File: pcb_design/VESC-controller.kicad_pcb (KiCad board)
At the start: 2 copper layers, 160 x 92.5 mm, 2 parts, among them U1 STM32F40X_LQFP64

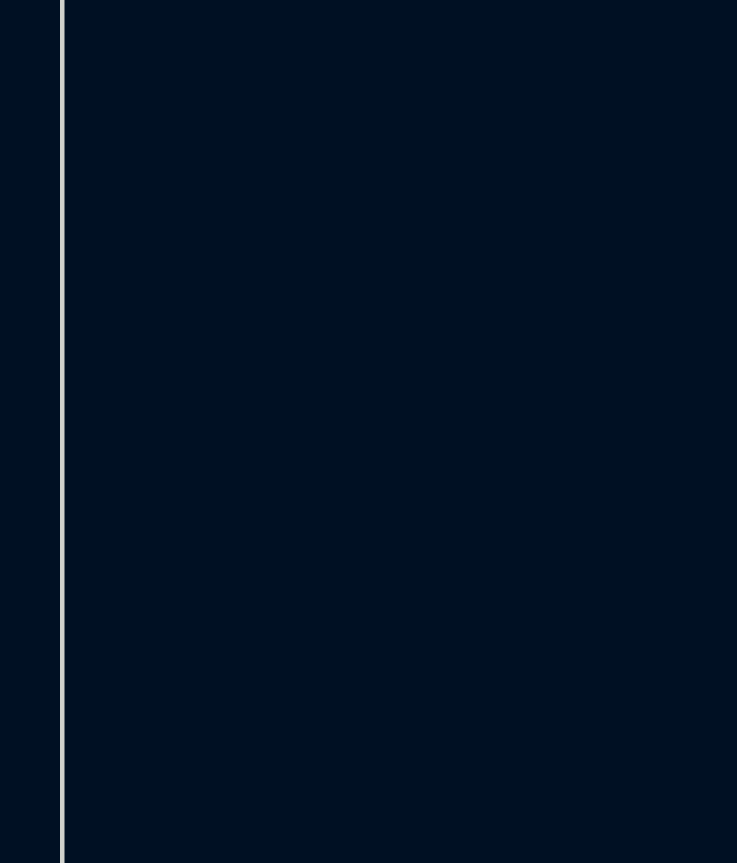
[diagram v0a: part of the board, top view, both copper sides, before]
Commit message: Added base VESC 4.xx schematic, added protection features, signal conditioning and pcb form factor
Signed-off-by: Marcos Chaparro <mchaparro@paltatech.com>
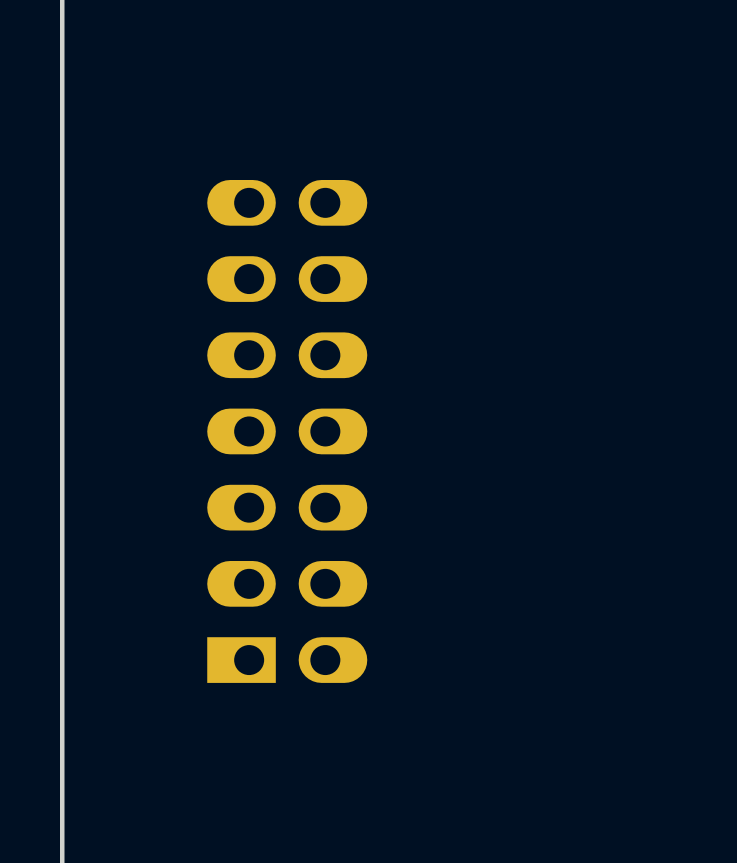
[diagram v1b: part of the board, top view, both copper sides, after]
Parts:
- added REF**: CONN-100MIL-M-2x7, conn-100mil:CONN-100MIL-M-2x7, B.Cu at (-72.5, 0.00)
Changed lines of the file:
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@@
     (links 0)
     (no_connects 0)
-    (area 0 0 0 0)
+    (area -80.275001 -45.275001 80.275001 47.775001)
     (thickness 1.6)
     (drawings 0)
     (tracks 0)
     (zones 0)
-    (modules 2)
+    (modules 3)
     (nets 65)
   )
@@
     (add_net "Net-(U1-Pad9)")
   )
+  (module conn-100mil:CONN-100MIL-M-2x7 (layer B.Cu)
+    (at -72.5 0 90)
+    (fp_text reference REF** (at 0 0 90) (layer B.SilkS)
+      (effects (font (size 0.8 0.8) (thickness 0.15)) (justify mirror))
+    )
+    (fp_text value CONN-100MIL-M-2x7 (at 0 0 90) (layer B.Fab)
+      (effects (font (size 0.8 0.8) (thickness 0.15)) (justify mirror))
+    )
+    (fp_line (start -9.525 -3.81) (end -6.35 -3.81) (layer B.SilkS) (width 0.15))
+    (fp_line (start -6.35 0) (end -6.35 -3.175) (layer B.Fab) (width 0.15))
+    (fp_line (start -9.525 0) (end -6.35 0) (layer B.Fab) (width 0.15))
+    (fp_line (start -6.35 0) (end -6.35 -3.175) (layer B.SilkS) (width 0.35))
+    (fp_line (start -9.525 0) (end -6.35 0) (layer B.SilkS) (width 0.35))
+    (fp_line (start -9.525 -3.175) (end -9.525 3.175) (layer B.SilkS) (width 0.35))
+    (fp_line (start 9.525 -3.175) (end -9.525 -3.175) (layer B.SilkS) (width 0.35))
+    (fp_line (start 9.525 3.175) (end 9.525 -3.175) (layer B.SilkS) (width 0.35))
+    (fp_line (start -9.525 3.175) (end 9.525 3.175) (layer B.SilkS) (width 0.35))
+    (fp_line (start -9.525 -3.175) (end -9.525 3.175) (layer B.Fab) (width 0.15))
+    (fp_line (start 9.525 -3.175) (end -9.525 -3.175) (layer B.Fab) (width 0.15))
+    (fp_line (start 9.525 3.175) (end 9.525 -3.175) (layer B.Fab) (width 0.15))
+    (fp_line (start -9.525 3.175) (end 9.525 3.175) (layer B.Fab) (width 0.15))
+    (fp_line (start -9.525 -3.175) (end -9.525 3.175) (layer B.CrtYd) (width 0.15))
+    (fp_line (start 9.525 -3.175) (end -9.525 -3.175) (layer B.CrtYd) (width 0.15))
+    (fp_line (start 9.525 3.175) (end 9.525 -3.175) (layer B.CrtYd) (width 0.15))
+    (fp_line (start -9.525 3.175) (end 9.525 3.175) (layer B.CrtYd) (width 0.15))
+    (pad 14 thru_hole oval (at 7.62 1.27 90) (size 1.524 2.286) (drill 1 (offset 0 0.254)) (layers *.Cu *.Mask B.SilkS))
+    (pad 12 thru_hole oval (at 5.08 1.27 90) (size 1.524 2.286) (drill 1 (offset 0 0.254)) (layers *.Cu *.Mask B.SilkS))
+    (pad 10 thru_hole oval (at 2.54 1.27 90) (size 1.524 2.286) (drill 1 (offset 0 0.254)) (layers *.Cu *.Mask B.SilkS))
+    (pad 8 thru_hole oval (at 0 1.27 90) (size 1.524 2.286) (drill 1 (offset 0 0.254)) (layers *.Cu *.Mask B.SilkS))
+    (pad 6 thru_hole oval (at -2.54 1.27 90) (size 1.524 2.286) (drill 1 (offset 0 0.254)) (layers *.Cu *.Mask B.SilkS))
+    (pad 4 thru_hole oval (at -5.08 1.27 90) (size 1.524 2.286) (drill 1 (offset 0 0.254)) (layers *.Cu *.Mask B.SilkS))
+    (pad 2 thru_hole oval (at -7.62 1.27 90) (size 1.524 2.286) (drill 1 (offset 0 0.254)) (layers *.Cu *.Mask B.SilkS))
+    (pad 13 thru_hole oval (at 7.62 -1.27 90) (size 1.524 2.286) (drill 1 (offset 0 -0.254)) (layers *.Cu *.Mask B.SilkS))
+    (pad 11 thru_hole oval (at 5.08 -1.27 90) (size 1.524 2.286) (drill 1 (offset 0 -0.254)) (layers *.Cu *.Mask B.SilkS))
+    (pad 9 thru_hole oval (at 2.54 -1.27 90) (size 1.524 2.286) (drill 1 (offset 0 -0.254)) (layers *.Cu *.Mask B.SilkS))
+    (pad 7 thru_hole oval (at 0 -1.27 90) (size 1.524 2.286) (drill 1 (offset 0 -0.254)) (layers *.Cu *.Mask B.SilkS))
+    (pad 5 thru_hole oval (at -2.54 -1.27 90) (size 1.524 2.286) (drill 1 (offset 0 -0.254)) (layers *.Cu *.Mask B.SilkS))
+    (pad 3 thru_hole oval (at -5.08 -1.27 90) (size 1.524 2.286) (drill 1 (offset 0 -0.254)) (layers *.Cu *.Mask B.SilkS))
+    (pad 1 thru_hole rect (at -7.62 -1.27 90) (size 1.524 2.286) (drill 1 (offset 0 -0.254)) (layers *.Cu *.Mask B.SilkS))
+    (model pin_strip/pin_strip_7x2.wrl
+      (at (xyz 0 0 0))
+      (scale (xyz 1 1 1))
+      (rotate (xyz 0 0 0))
+    )
+  )
   (module IPC7351-Nominal:QFP50P1200X1200X100-64 (layer F.Cu)

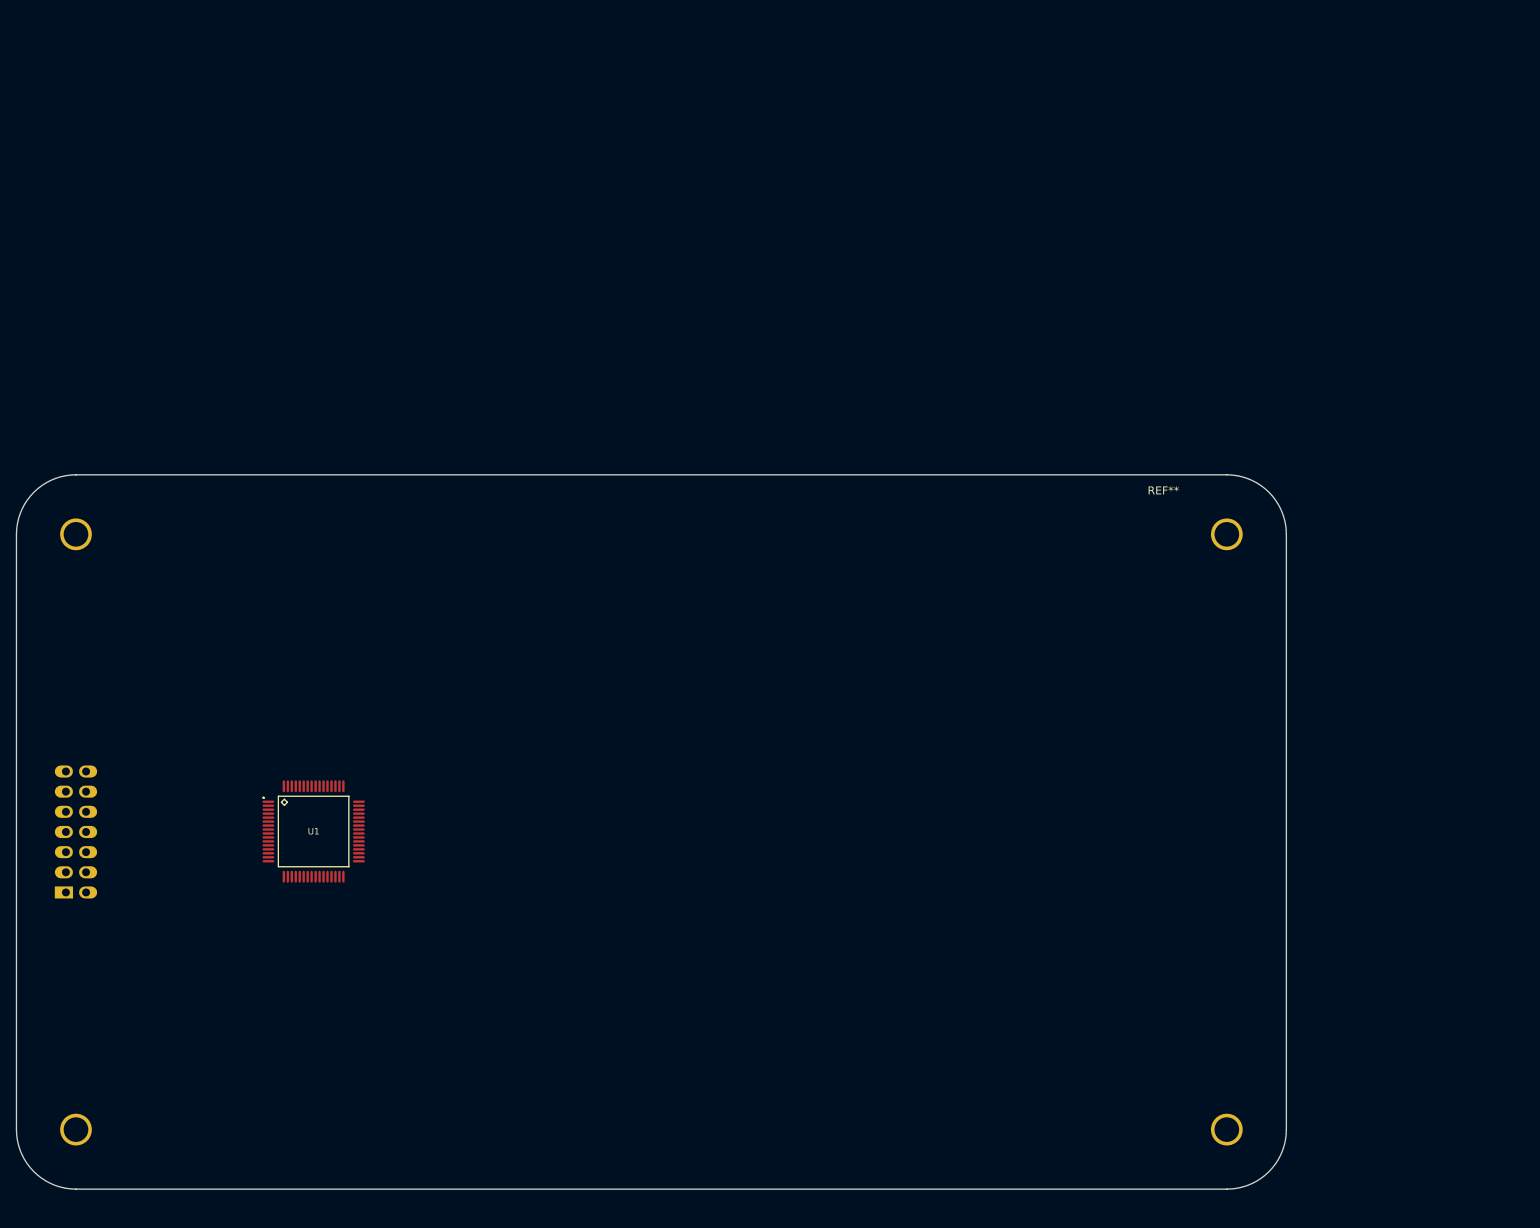
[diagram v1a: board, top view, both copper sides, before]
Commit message: Updated MCU sheet to comply with VESC 6 pinout. Added 5v analog inputs and updated some labels
Signed-off-by: Marcos Chaparro <mchaparro@paltatech.com>
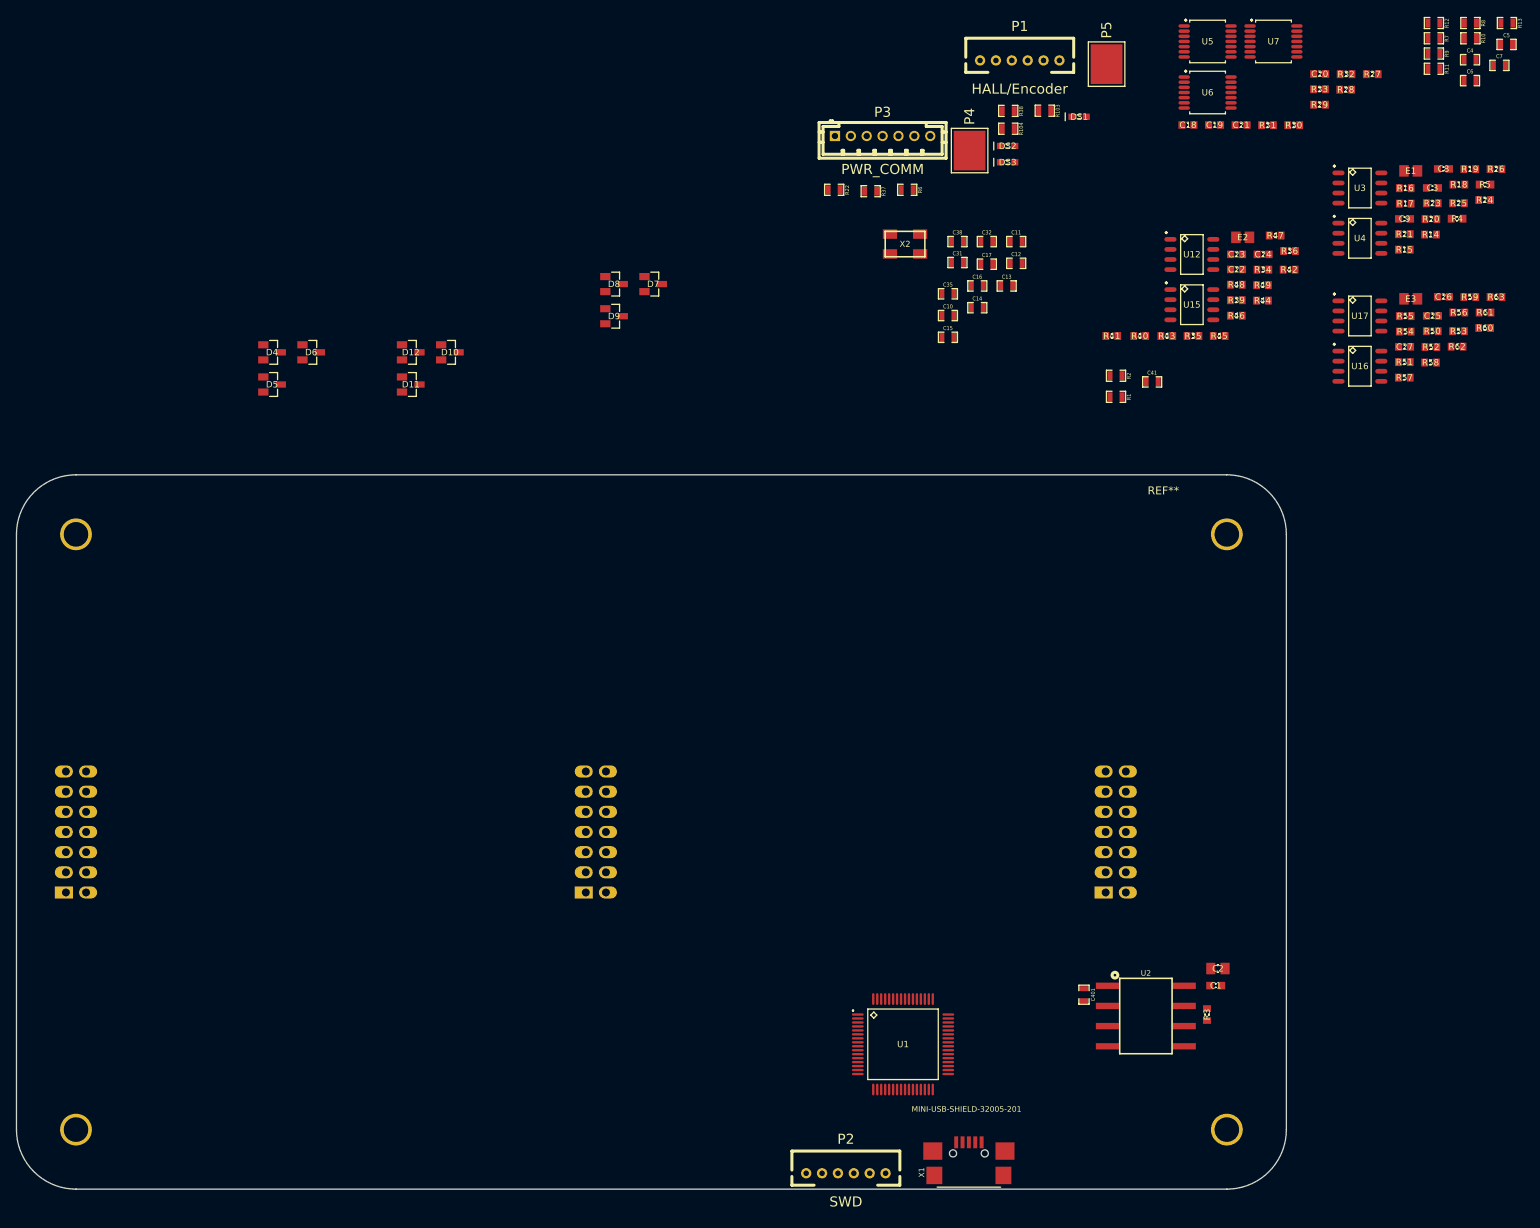
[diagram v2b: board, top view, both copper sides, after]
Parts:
- removed the REF** at (-72.5, 0.00)
- added C1: 100nF, IPC7351-Nominal:CAPC1608X55, F.Cu at (71.1, 19.4)
- added C10: 2.2u, CRF1:SMD-0603_c, F.Cu at (37.4, -65.1)
- added C11: 2.2u, CRF1:SMD-0603_c, F.Cu at (46.0, -74.4)
- added C12: 2.2u, CRF1:SMD-0603_c, F.Cu at (46.0, -71.6)
- added C13: 2.2u, CRF1:SMD-0603_c, F.Cu at (44.8, -68.8)
- added C14: 2.2u, CRF1:SMD-0603_c, F.Cu at (41.1, -66.1)
- added C15: 15p, CRF1:SMD-0603_c, F.Cu at (37.4, -62.3)
- added C16: 2.2u, CRF1:SMD-0603_c, F.Cu at (41.1, -68.8)
- added C17: 2.2u, CRF1:SMD-0603_c, F.Cu at (42.3, -71.5)
- added C18: 100nF, IPC7351-Nominal:CAPC1608X55, F.Cu at (67.6, -89.1)
- added C19: 100nF, IPC7351-Nominal:CAPC1608X55, F.Cu at (70.9, -89.1)
- added C2: 10uF, IPC7351-Nominal:CAPC2012X70, F.Cu at (71.4, 17.2)
- added C20: 100nF, IPC7351-Nominal:CAPC1608X55, F.Cu at (84.2, -95.5)
- added C21: 100nF, IPC7351-Nominal:CAPC1608X55, F.Cu at (74.3, -89.1)
- added C22: 100nF, IPC7351-Nominal:CAPC1608X55, F.Cu at (73.7, -70.9)
- added C23: 100pF, IPC7351-Nominal:CAPC1608X55, F.Cu at (73.7, -72.8)
- added C24: 100nF, IPC7351-Nominal:CAPC1608X55, F.Cu at (77.1, -72.8)
- added C25: 100nF, IPC7351-Nominal:CAPC1608X55, F.Cu at (98.4, -65.0)
- added C26: 100pF, IPC7351-Nominal:CAPC1608X55, F.Cu at (99.8, -67.4)
- added C27: 100nF, IPC7351-Nominal:CAPC1608X55, F.Cu at (94.9, -61.1)
- added C3: 100nF, IPC7351-Nominal:CAPC1608X55, F.Cu at (98.4, -81.1)
- added C31: 2.2u, CRF1:SMD-0603_c, F.Cu at (38.6, -71.7)
- added C32: 100n, CRF1:SMD-0603_c, F.Cu at (42.3, -74.4)
- added C35: 2.2u, CRF1:SMD-0603_c, F.Cu at (37.4, -67.8)
- added C38: 15p, CRF1:SMD-0603_c, F.Cu at (38.6, -74.4)
- added C4: 4n7, CRF1:SMD-0603_c, F.Cu at (103.1, -97.3)
- added C401: 2.2u, CRF1:SMD-0603_c, F.Cu at (54.5, 20.5)
- added C41: 2.2u, CRF1:SMD-0603_c, F.Cu at (63.1, -56.7)
- added C5: 4n7, CRF1:SMD-0603_c, F.Cu at (107.7, -99.2)
- added C6: 4n7, CRF1:SMD-0603_c, F.Cu at (103.1, -94.7)
- added C7: 4n7, CRF1:SMD-0603_c, F.Cu at (106.8, -96.6)
- added C8: 100pF, IPC7351-Nominal:CAPC1608X55, F.Cu at (99.8, -83.5)
- added C9: 100nF, IPC7351-Nominal:CAPC1608X55, F.Cu at (94.9, -77.2)
- added D10: BAT54S, smd-semi:SOT-23, F.Cu at (-25.4, -60.4)
- added D11: BAT54S, smd-semi:SOT-23, F.Cu at (-30.3, -56.4)
- added D12: BAT54S, smd-semi:SOT-23, F.Cu at (-30.3, -60.4)
- added D4: BAT54S, smd-semi:SOT-23, F.Cu at (-47.8, -60.4)
- added D5: BAT54S, smd-semi:SOT-23, F.Cu at (-47.8, -56.4)
- added D6: BAT54S, smd-semi:SOT-23, F.Cu at (-42.9, -60.4)
- added D7: BAT54S, smd-semi:SOT-23, F.Cu at (0.22, -69.0)
- added D8: BAT54S, smd-semi:SOT-23, F.Cu at (-4.71, -69.0)
- added D9: BAT54S, smd-semi:SOT-23, F.Cu at (-4.71, -65.0)
- added DS1: RED, smd-semi:LED-0603, F.Cu at (53.9, -90.1)
- added DS2: GREEN, smd-semi:LED-0603, F.Cu at (44.9, -86.4)
- added DS3: GREEN, smd-semi:LED-0603, F.Cu at (44.9, -84.4)
- added E1: BEAD-0805, IPC7351-Nominal:INDC2012X130, F.Cu at (95.7, -83.3)
- added E2: BEAD-0805, IPC7351-Nominal:INDC2012X130, F.Cu at (74.5, -74.9)
- added E3: BEAD-0805, IPC7351-Nominal:INDC2012X130, F.Cu at (95.7, -67.2)
- added J1: GATE_DRIVER_CONN_U, conn-100mil:CONN-100MIL-M-2x7, B.Cu at (-72.5, 0.00)
- added J2: GATE_DRIVER_CONN_V, conn-100mil:CONN-100MIL-M-2x7, B.Cu at (-7.00, 0.00)
- added J3: GATE_DRIVER_CONN_W, conn-100mil:CONN-100MIL-M-2x7, B.Cu at (58.5, 0.00)
- added P1: HALL/Encoder, CRF1:MICRO_JST_6, F.Cu at (46.4, -97.2)
- added P2: SWD, CRF1:MICRO_JST_6, F.Cu at (24.5, 43.0)
- added P3: PWR_COMM, CRF1:b7b-ph-kl, F.Cu at (29.1, -87.7)
- added P4: IN+, CRF1:1PAD_4x5mm, F.Cu at (40.1, -85.9)
- added P5: IN-, CRF1:1PAD_4x5mm, F.Cu at (57.3, -96.7)
- added R1: NTC 10k, CRF1:SMD-0603_r, F.Cu at (58.5, -54.8)
- added R10: 10k, CRF1:SMD-0603_r, F.Cu at (103.2, -100.0)
- added R103: 22R, CRF1:SMD-0603_r, F.Cu at (49.6, -90.9)
- added R104: 22R, CRF1:SMD-0603_r, F.Cu at (45.0, -88.6)
- added R11: 2k2, CRF1:SMD-0603_r, F.Cu at (98.6, -96.2)
- added R12: 2k2, CRF1:SMD-0603_r, F.Cu at (98.6, -101.9)
- added R13: 2k2, CRF1:SMD-0603_r, F.Cu at (107.8, -101.9)
- added R14: 10k, IPC7351-Nominal:RESC1608X50, F.Cu at (98.2, -75.3)
- added R15: 10k, IPC7351-Nominal:RESC1608X50, F.Cu at (94.9, -73.4)
- added R16: R-0603, IPC7351-Nominal:RESC1608X50, F.Cu at (95.0, -81.1)
- added R17: R-0603, IPC7351-Nominal:RESC1608X50, F.Cu at (95.0, -79.2)
- added R18: 10k, IPC7351-Nominal:RESC1608X50, F.Cu at (101.7, -81.6)
- added R19: 10k, IPC7351-Nominal:RESC1608X50, F.Cu at (103.1, -83.5)
- added R2: 10k, CRF1:SMD-0603_r, F.Cu at (58.5, -57.5)
- added R20: 22R, IPC7351-Nominal:RESC1608X50, F.Cu at (98.2, -77.2)
- added R21: 22R, IPC7351-Nominal:RESC1608X50, F.Cu at (94.9, -75.3)
- added R22: 2k2, CRF1:SMD-0603_r, F.Cu at (23.0, -80.9)
- added R23: 1k, IPC7351-Nominal:RESC1608X50, F.Cu at (98.4, -79.2)
- added R24: 10k, IPC7351-Nominal:RESC1608X50, F.Cu at (105.0, -79.6)
- added R25: 10k, IPC7351-Nominal:RESC1608X50, F.Cu at (101.7, -79.2)
- added R26: 4.7k, IPC7351-Nominal:RESC1608X50, F.Cu at (106.4, -83.5)
- added R27: 4.7k, IPC7351-Nominal:RESC1608X50, F.Cu at (90.8, -95.5)
- added R28: 4.7k, IPC7351-Nominal:RESC1608X50, F.Cu at (87.5, -93.5)
- added R29: 4.7k, IPC7351-Nominal:RESC1608X50, F.Cu at (84.2, -91.6)
- added R3: 120R, IPC7351-Nominal:RESC1608X50, F.Cu at (70.0, 23.0)
- added R30: 4.7k, IPC7351-Nominal:RESC1608X50, F.Cu at (80.9, -89.0)
- added R31: 4.7k, IPC7351-Nominal:RESC1608X50, F.Cu at (77.6, -89.0)
- added R32: 4.7k, IPC7351-Nominal:RESC1608X50, F.Cu at (87.5, -95.5)
- added R33: 4.7k, IPC7351-Nominal:RESC1608X50, F.Cu at (84.2, -93.6)
- added R34: 10k, IPC7351-Nominal:RESC1608X50, F.Cu at (77.0, -70.8)
- added R35: 10k, IPC7351-Nominal:RESC1608X50, F.Cu at (68.2, -62.5)
- added R36: 10k, IPC7351-Nominal:RESC1608X50, F.Cu at (80.4, -73.2)
- added R37: 100R, CRF1:SMD-0603_r, F.Cu at (27.6, -80.7)
- added R38: 100R, CRF1:SMD-0603_r, F.Cu at (45.0, -90.9)
- added R39: 10k, IPC7351-Nominal:RESC1608X50, F.Cu at (73.7, -67.0)
- added R4: 10k, IPC7351-Nominal:RESC1608X50, F.Cu at (101.5, -77.3)
- added R40: R-0603, IPC7351-Nominal:RESC1608X50, F.Cu at (61.5, -62.5)
- added R41: R-0603, IPC7351-Nominal:RESC1608X50, F.Cu at (58.0, -62.5)
- added R42: 10k, IPC7351-Nominal:RESC1608X50, F.Cu at (80.3, -70.8)
- added R43: 10k, IPC7351-Nominal:RESC1608X50, F.Cu at (64.9, -62.5)
- added R44: 22R, IPC7351-Nominal:RESC1608X50, F.Cu at (77.0, -66.9)
- added R45: 22R, IPC7351-Nominal:RESC1608X50, F.Cu at (71.5, -62.5)
- added R46: 1k, IPC7351-Nominal:RESC1608X50, F.Cu at (73.7, -65.0)
- added R47: 10k, IPC7351-Nominal:RESC1608X50, F.Cu at (78.6, -75.1)
- added R48: 10k, IPC7351-Nominal:RESC1608X50, F.Cu at (73.7, -68.9)
- added R49: 4.7k, IPC7351-Nominal:RESC1608X50, F.Cu at (77.0, -68.9)
- added R5: 10k, IPC7351-Nominal:RESC1608X50, F.Cu at (105.0, -81.6)
- added R50: 10k, IPC7351-Nominal:RESC1608X50, F.Cu at (98.4, -63.1)
- added R51: 10k, IPC7351-Nominal:RESC1608X50, F.Cu at (94.9, -59.2)
- added R52: 10k, IPC7351-Nominal:RESC1608X50, F.Cu at (98.2, -61.1)
- added R53: 10k, IPC7351-Nominal:RESC1608X50, F.Cu at (101.7, -63.1)
- added R54: R-0603, IPC7351-Nominal:RESC1608X50, F.Cu at (95.0, -63.0)
- added R55: R-0603, IPC7351-Nominal:RESC1608X50, F.Cu at (95.0, -65.0)
- added R56: 10k, IPC7351-Nominal:RESC1608X50, F.Cu at (101.7, -65.4)
- added R57: 10k, IPC7351-Nominal:RESC1608X50, F.Cu at (94.9, -57.2)
- added R58: 22R, IPC7351-Nominal:RESC1608X50, F.Cu at (98.2, -59.1)
- added R59: 22R, IPC7351-Nominal:RESC1608X50, F.Cu at (103.1, -67.4)
- added R6: 0R, CRF1:SMD-0603_r, F.Cu at (32.2, -80.9)
- added R60: 1k, IPC7351-Nominal:RESC1608X50, F.Cu at (105.0, -63.5)
- added R61: 10k, IPC7351-Nominal:RESC1608X50, F.Cu at (105.0, -65.4)
- added R62: 10k, IPC7351-Nominal:RESC1608X50, F.Cu at (101.5, -61.1)
- added R63: 4.7k, IPC7351-Nominal:RESC1608X50, F.Cu at (106.4, -67.4)
- added R7: 10k, CRF1:SMD-0603_r, F.Cu at (98.6, -100.0)
- added R8: 10k, CRF1:SMD-0603_r, F.Cu at (103.2, -101.9)
- added R9: 10k, CRF1:SMD-0603_r, F.Cu at (98.6, -98.1)
- added U12: OPA2376AID, IPC7351-Nominal:SOIC127P600X175-8, F.Cu at (68.1, -72.8)
- added U15: OPA2376AID, IPC7351-Nominal:SOIC127P600X175-8, F.Cu at (68.1, -66.4)
- added U16: OPA2376AID, IPC7351-Nominal:SOIC127P600X175-8, F.Cu at (89.3, -58.7)
- added U17: LM2903-SO8, IPC7351-Nominal:SOIC127P600X175-8, F.Cu at (89.3, -65.0)
- added U2: ISO1050, paltatech:SO8-ISO1050, F.Cu at (62.3, 23.2)
- added U3: OPA2376AID, IPC7351-Nominal:SOIC127P600X175-8, F.Cu at (89.3, -81.1)
- added U4: LM2903-SO8, IPC7351-Nominal:SOIC127P600X175-8, F.Cu at (89.3, -74.8)
- added U5: 7400-TSSOP, IPC7351-Nominal:SOP65P640X110-14, F.Cu at (70.1, -99.6)
- added U6: SN74ALVC08PWR, IPC7351-Nominal:SOP65P640X110-14, F.Cu at (70.1, -93.2)
- added U7: SN74ALVC08PWR, IPC7351-Nominal:SOP65P640X110-14, F.Cu at (78.4, -99.6)
- added X1: MINI-USB-SHIELD-32005-201, paltatech:USB-UX60R-MB-5ST, F.Cu at (40.0, 40.5)
- added X2: 8MHz 10ppm, CRF1:Crystal_5x3mm, F.Cu at (32.0, -74.1)
- moved U1 79.0 mm to (31.7, 26.8)
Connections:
- net Net-(U1-Pad10) renamed /MCU/AN_IN
- net Net-(U1-Pad14) renamed /MCU/SENS3
- net Net-(U1-Pad15) renamed /MCU/SENS2
- net Net-(U1-Pad16) renamed /MCU/SENS1
- net Net-(U1-Pad26) renamed /MCU/BR_SO2
- net Net-(U1-Pad27) renamed /MCU/BR_SO1
- net Net-(U1-Pad33) renamed /MCU/DC_CAL
- net Net-(U1-Pad34) renamed /MCU/L3
- net Net-(U1-Pad35) renamed /MCU/L2
- net Net-(U1-Pad36) renamed /MCU/L1
- net Net-(U1-Pad41) renamed /MCU/H3
- net Net-(U1-Pad42) renamed /MCU/H2
- net Net-(U1-Pad43) renamed /MCU/H1
- net Net-(U1-Pad51) renamed /MCU/EN_GATE
- net Net-(U1-Pad53) renamed /MCU/FAULT
- net Net-(U1-Pad57) renamed /MCU/SERVO
- U1 pad 1: Net-(U1-Pad1) -> VCC
- U1 pad 12: Net-(U1-Pad12) -> GND
- U1 pad 13: Net-(U1-Pad13) -> VCC
- U1 pad 17: Net-(U1-Pad17) -> /MCU/ADC_TEMP
- U1 pad 18: Net-(U1-Pad18) -> GND
- U1 pad 19: Net-(U1-Pad19) -> VCC
- U1 pad 20: Net-(U1-Pad20) -> /TX_SDA
- U1 pad 21: Net-(U1-Pad21) -> /SCK_ADC_EXT
- U1 pad 22: Net-(U1-Pad22) -> /MISO_RX_SCL
- U1 pad 23: Net-(U1-Pad23) -> /RX_SCL_MOSI
- U1 pad 24: Net-(U1-Pad24) -> /MCU/LED_GREEN
- U1 pad 25: Net-(U1-Pad25) -> /MCU/LED_RED
- U1 pad 29: Net-(U1-Pad29) -> /RX_SCL_MOSI
- U1 pad 30: Net-(U1-Pad30) -> /TX_SDA
- U1 pad 32: Net-(U1-Pad32) -> VCC
- U1 pad 37: Net-(U1-Pad37) -> /TX_SDA
- U1 pad 38: Net-(U1-Pad38) -> /RX_SCL_MOSI
- U1 pad 44: Net-(U1-Pad44) -> /MCU/USB_DM
- U1 pad 45: Net-(U1-Pad45) -> /MCU/USB_DP
- U1 pad 46: Net-(U1-Pad46) -> SWDIO
- U1 pad 48: Net-(U1-Pad48) -> VCC
- U1 pad 49: Net-(U1-Pad49) -> SWCLK
- U1 pad 52: Net-(U1-Pad52) -> /Filters/HALL3_OUT
- U1 pad 58: Net-(U1-Pad58) -> /Filters/HALL1_OUT
- U1 pad 59: Net-(U1-Pad59) -> /Filters/HALL2_OUT
- U1 pad 60: Net-(U1-Pad60) -> GND
- U1 pad 61: Net-(U1-Pad61) -> /Isolated CAN/CAN_RX
- U1 pad 62: Net-(U1-Pad62) -> /Isolated CAN/CAN_TX
- U1 pad 63: Net-(U1-Pad63) -> GND
- U1 pad 64: Net-(U1-Pad64) -> VCC
- U1 pad 7: Net-(U1-Pad7) -> NRST
- U1 pad 8: Net-(U1-Pad8) -> /Filters/TEMP_IN
